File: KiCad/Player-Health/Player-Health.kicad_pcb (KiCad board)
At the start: 2 copper layers, 34 parts, among them IC1 ATMEGA328-P, J1 MICRO_USB, M1 RUMBLE, P1 2P_CGRID_M, P2 6pM CGrid, P3 6pM Header, P4 8pF Header, Q1 NPN, U1 MCP73831, U2 LM1084IT-3.3/NOPB, U3 14SLED, U4 ESP8266, X1 CRYSTAL

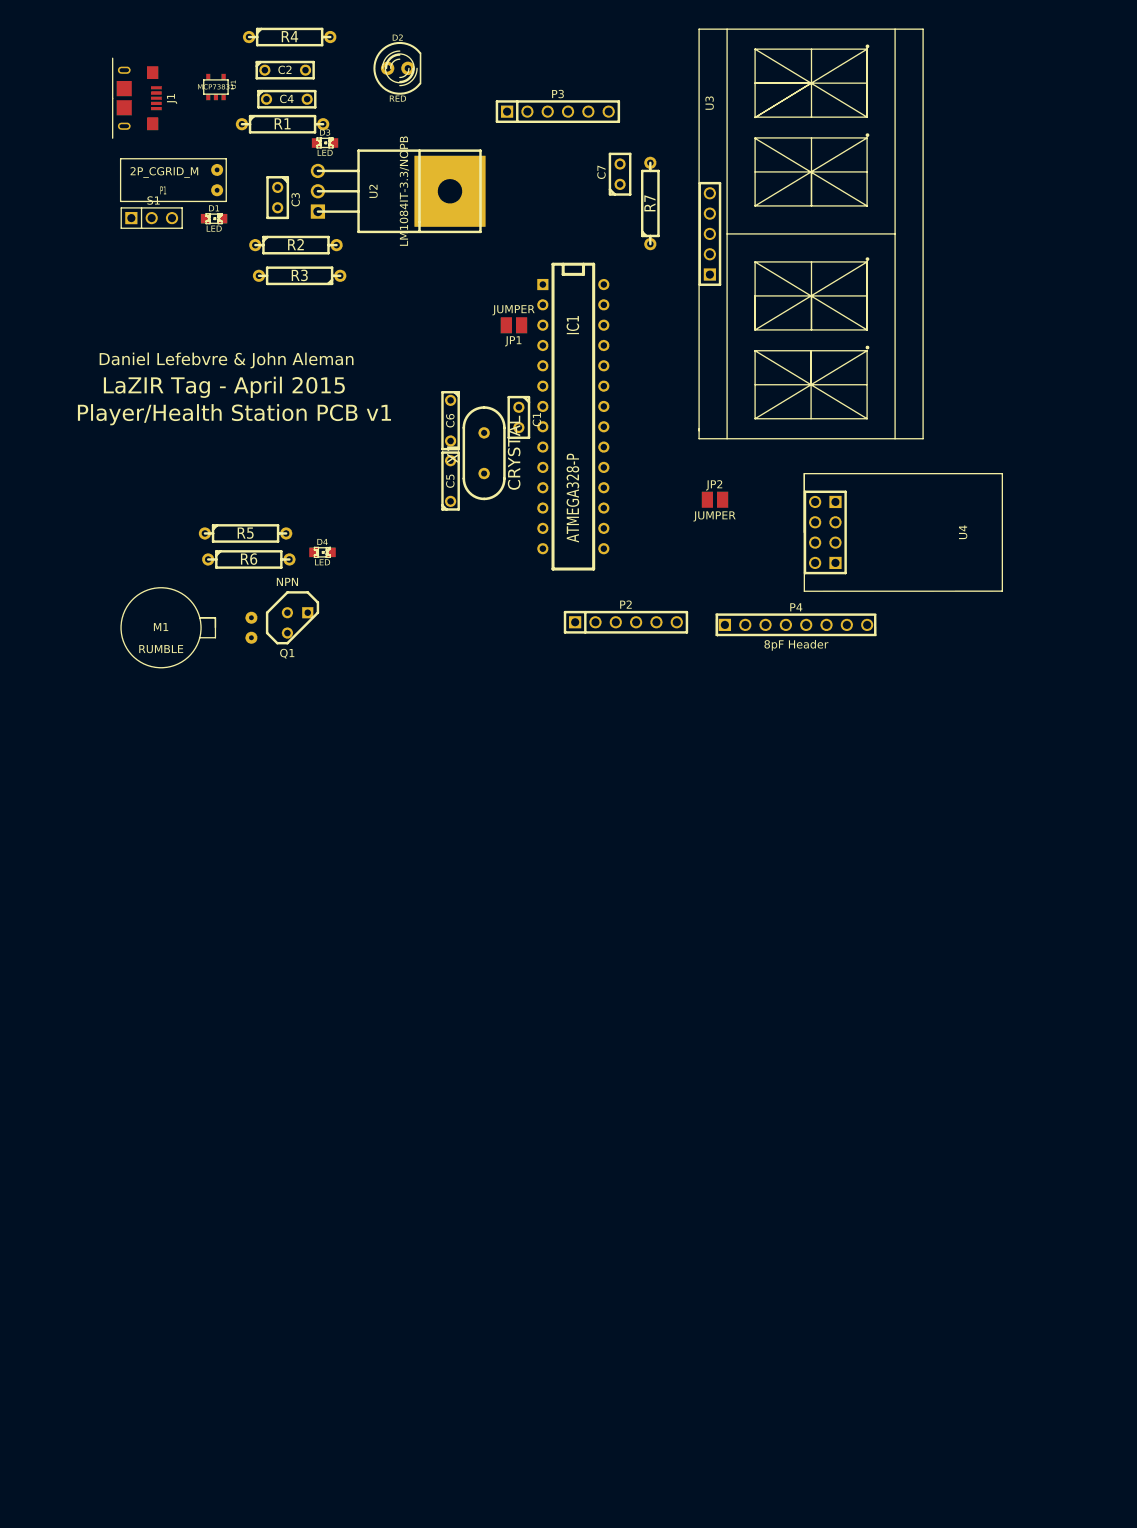
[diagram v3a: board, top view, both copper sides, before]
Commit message: Update #1 4/17
First Draft of Player/Health PCB for review.
Added on/off indicators to weapon pcb for slideswitch
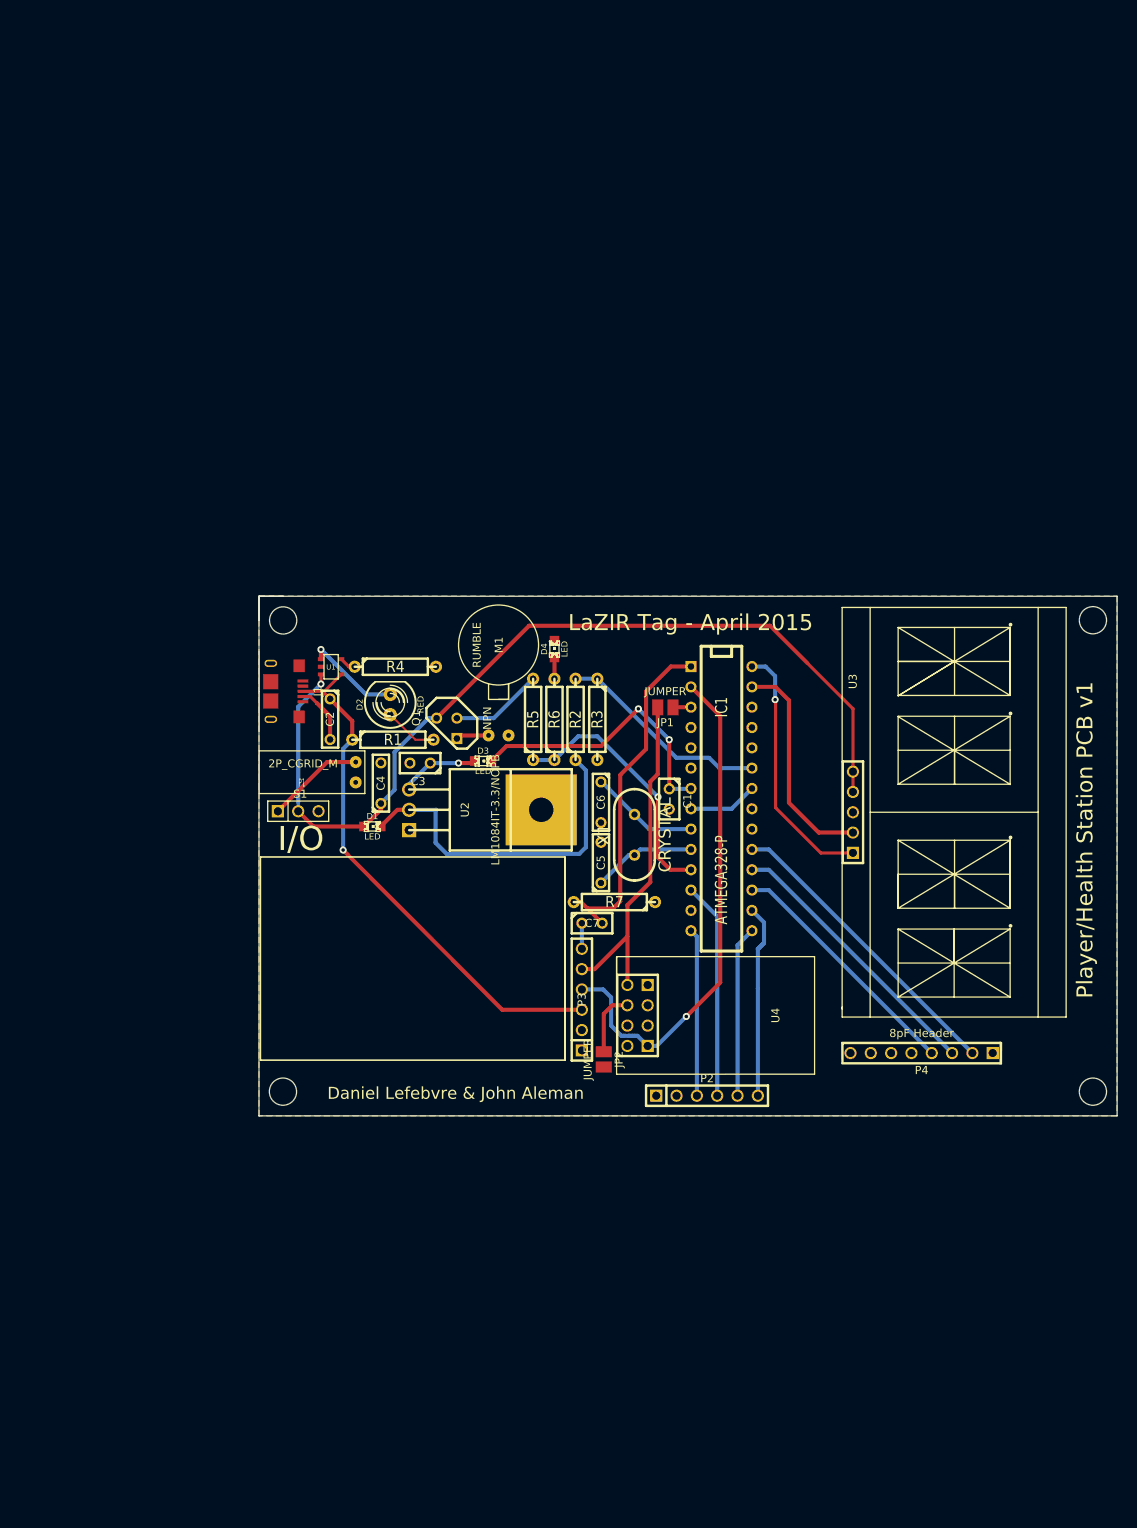
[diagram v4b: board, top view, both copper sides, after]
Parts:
- moved P3 111.0 mm to (80.7, 137.1), turned to 90 degrees
- moved C7 93.7 mm to (82.0, 127.5), turned to 0 degrees
- moved R7 87.4 mm to (84.8, 124.9), turned to 180 degrees
- moved C4 86.3 mm to (55.6, 110.0), turned to 90 degrees
- moved C2 81.3 mm to (49.3, 102.0), turned to 270 degrees
- moved R4 79.8 mm to (57.4, 95.5)
- moved D3 79.8 mm to (68.4, 107.3)
- moved D2 79.5 mm to (56.8, 100.2), turned to 90 degrees
- moved D1 78.5 mm to (54.5, 115.4)
- moved R1 78.2 mm to (57.1, 104.6)
- moved U2 78.2 mm to (59.1, 113.4)
- moved J1 76.4 mm to (41.8, 98.6)
- moved S1 76.4 mm to (45.3, 113.5)
- moved P1 76.0 mm to (52.5, 108.7)
- moved U3 74.5 mm to (114.6, 113.7)
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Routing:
- net VBatt: track 0.00 -> 116.7 mm, vias 0 -> 1
- net UART RX: track 0.00 -> 65.9 mm, vias 0 -> 1
- net USBV: track 0.00 -> 65.7 mm, vias 0 -> 1
- net UART TX: track 0.00 -> 43.6 mm
- net Reset: track 0.00 -> 43.6 mm
- net N-000006: track 0.00 -> 43.1 mm
- net SCK: track 0.00 -> 38.1 mm
- net +3.3V: track 0.00 -> 35.4 mm, vias 0 -> 2
- net MISO: track 0.00 -> 34.5 mm
- net Rumble: track 0.00 -> 32.3 mm, vias 0 -> 1
- net I2C CLK: track 0.00 -> 31.9 mm, vias 0 -> 1
- net MOSI: track 0.00 -> 30.9 mm
- net I2C DAT: track 0.00 -> 27.7 mm
- net LED G: track 0.00 -> 27.1 mm
- net VSense: track 0.00 -> 26.7 mm
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- added copper zone on B.Cu, net +3.3V
- added copper zone on F.Cu, net GND
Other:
- board outline added: 107.3 x 64.9 mm
- net class Default: trace_width 0.254 -> 0.391
- board text added: "I/O"

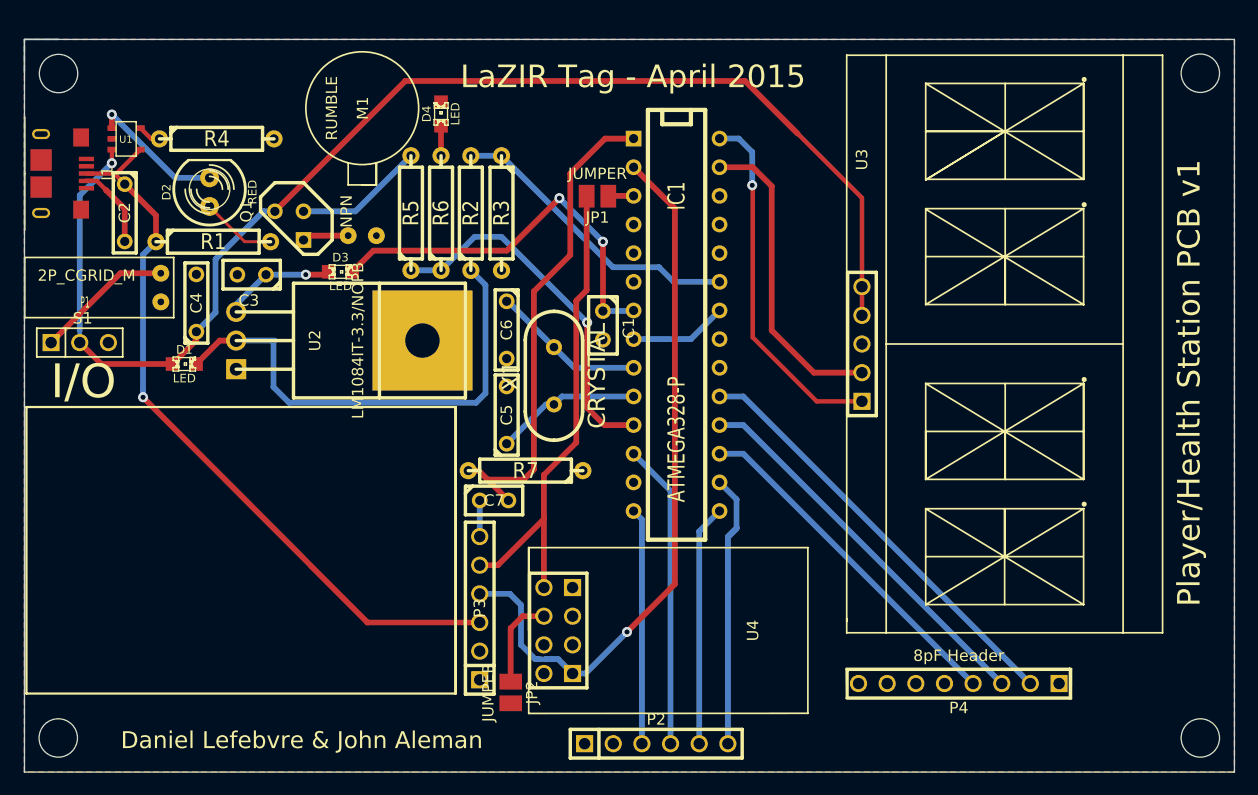
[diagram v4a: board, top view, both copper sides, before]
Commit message: Update #2 4/17
Shrunk board to be >10cm
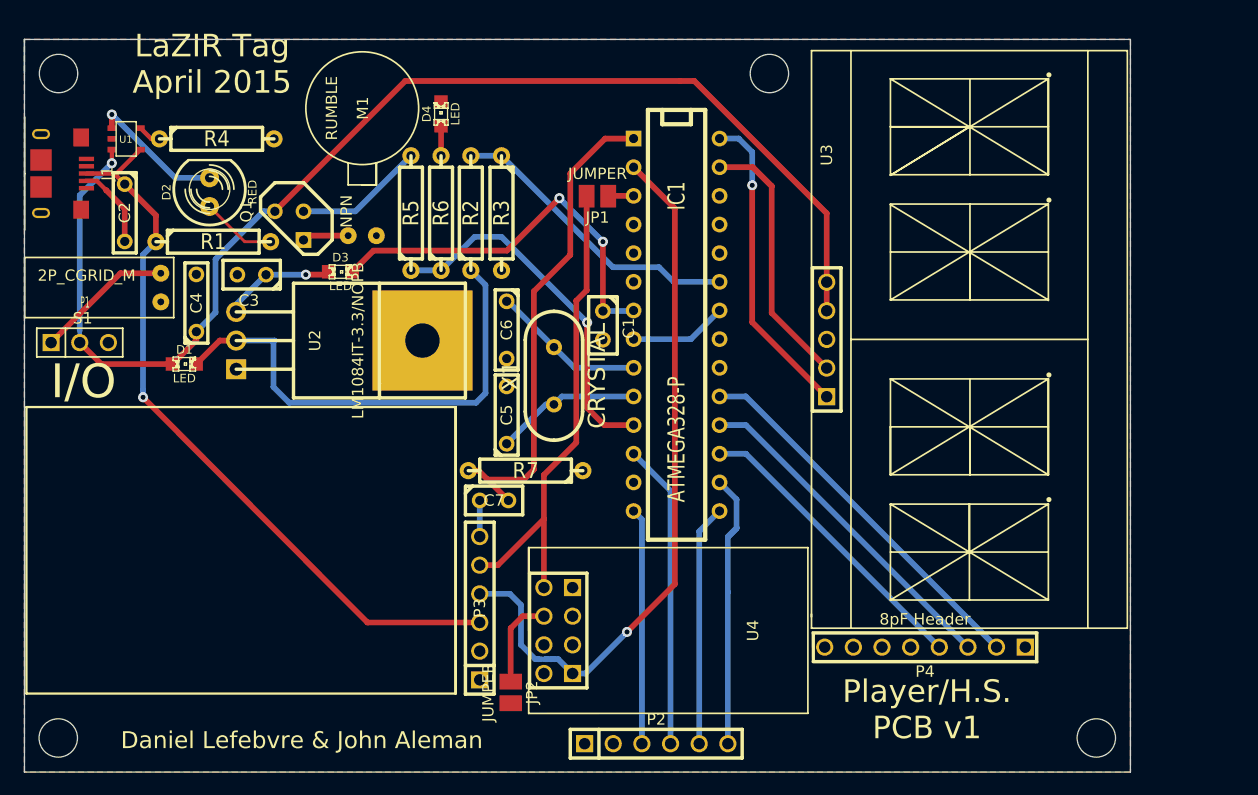
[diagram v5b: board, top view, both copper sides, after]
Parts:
- moved P4 4.40 mm to (120.2, 140.5)
- moved U3 3.15 mm to (111.5, 113.3)
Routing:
- net SCK: track 38.1 -> 65.2 mm
- net MISO: track 34.5 -> 58.0 mm
- net MOSI: track 30.9 -> 50.8 mm
- net VBatt: track 116.7 -> 129.0 mm
- net I2C CLK: track 31.9 -> 27.8 mm
- net I2C DAT: track 27.7 -> 25.8 mm
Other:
- board size 107.3 x 64.9 mm -> 98 x 64.9 mm
- net class Default: trace_width 0.391 -> 0.508
- board text added: "LaZIR Tag April 2015"
- board text added: "Player/H.S. PCB v1"
- board text removed: "LaZIR Tag - April 2015"
- board text removed: "Player/Health Station PCB v1"

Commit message: Quick Update #1 4/24
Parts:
- added R8: 220, R4, F.Cu at (87.9, 92.7)
- moved D3 22.4 mm to (87.5, 95.6)
- moved P4 5.01 mm to (124.7, 142.8)
- moved S1 0.05 mm to (45.3, 113.6)
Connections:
- C3 pad 1: N-0000028 -> +3.3V
- D3 pad 1: N-0000028 -> +3.3V
- D3 pad 2: +3.3V -> N-0000023
- U2 pad 2: N-0000028 -> +3.3V
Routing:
- net SCK: track 65.2 -> 39.2 mm
- net MISO: track 58.0 -> 35.6 mm
- net MOSI: track 50.8 -> 32.0 mm
- net +3.3V: track 35.4 -> 53.2 mm, vias 2 -> 3
- net N-0000028: track 10.1 -> 0.00 mm, vias 1 -> 0
- net N-0000023: track 0.00 -> 5.64 mm

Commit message: Quick Update #2 4/24
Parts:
- removed D1: LED, LED-0805
- moved S1 1.40 mm to (45.3, 115.0)
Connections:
- R2 pad 1: N-000005 (its old number) -> VBatt
- R3 pad 1: VSense -> (no net)
- U2 pad 3: N-000005 (its old number) -> VBatt
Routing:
- net VBatt: track 129.0 -> 172.4 mm
- net N-000005 (its old number): track 43.1 -> 0.00 mm
- net N-000005: track 12.3 -> 13.7 mm

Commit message: Quick Update #3 4/24
Adjusted keepout areas
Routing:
- net GND: track 16.0 -> 27.6 mm
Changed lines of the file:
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@@
     (links 76)
     (no_connects 0)
-    (area 39.053912 86.614799 138.459601 152.1206)
+    (area 39.104712 86.614799 138.459601 152.1206)
     (thickness 1.6)
     (drawings 23)
-    (tracks 183)
+    (tracks 186)
     (zones 0)
     (modules 34)
@@
   (segment (start 61.7728 107.5182) (end 65.3034 107.5182) (width 0.508) (layer B.Cu) (net 1))
   (via (at 65.3034 107.5182) (size 0.889) (layers F.Cu B.Cu) (net 1))
+  (segment (start 59.1312 115.9002) (end 54.2544 115.9002) (width 0.508) (layer B.Cu) (net 2) (status 400000))
+  (segment (start 52.451 114.0968) (end 52.451 109.9312) (width 0.508) (layer B.Cu) (net 2) (status 800000))
+  (segment (start 54.2544 115.9002) (end 52.451 114.0968) (width 0.508) (layer B.Cu) (net 2))
   (segment (start 94.361 113.2332) (end 99.441 113.2332) (width 0.508) (layer B.Cu) (net 2))
   (segment (start 99.441 113.2332) (end 101.981 110.6932) (width 0.508) (layer B.Cu) (net 2))
@@
       )
     )
+  )
+  (zone (net 0) (net_name "") (layer B.Cu) (hatch edge 0.508)
+    (connect_pads (clearance 0.508))
+    (min_thickness 0.254)
+    (keepout (tracks not_allowed) (vias not_allowed) (copperpour not_allowed))
+    (fill (arc_segments 16) (thermal_gap 0.508) (thermal_bridge_width 0.508))
+    (polygon
+      (pts
+        (xy 80.6704 133.223) (xy 80.7466 127.762) (xy 85.7504 125.8062) (xy 85.979 128.8034) (xy 81.9404 133.1722)
+      )
+    )
+  )
+  (zone (net 0) (net_name "") (layer F.Cu) (hatch edge 0.508)
+    (connect_pads (clearance 0.508))
+    (min_thickness 0.254)
+    (keepout (tracks not_allowed) (vias not_allowed) (copperpour not_allowed))
+    (fill (arc_segments 16) (thermal_gap 0.508) (thermal_bridge_width 0.508))
+    (polygon
+      (pts
+        (xy 80.6704 133.223) (xy 80.7466 127.762) (xy 85.7504 125.8062) (xy 85.979 128.8034) (xy 81.9404 133.1722)
+      )
+    )
+  )
+  (zone (net 0) (net_name "") (layer B.Cu) (hatch edge 0.508)
+    (connect_pads (clearance 0.508))
+    (min_thickness 0.254)
+    (keepout (tracks not_allowed) (vias not_allowed) (copperpour not_allowed))
+    (fill (arc_segments 16) (thermal_gap 0.508) (thermal_bridge_width 0.508))
+    (polygon
+      (pts
+        (xy 42.9514 115.0874) (xy 42.9514 113.538) (xy 49.022 107.4674) (xy 51.3588 107.4166) (xy 51.0032 112.4458)
+        (xy 47.0408 112.4966) (xy 45.2374 114.9604)
+      )
+    )
+  )
+  (zone (net 0) (net_name "") (layer F.Cu) (hatch edge 0.508)
+    (connect_pads (clearance 0.508))
+    (min_thickness 0.254)
+    (keepout (tracks not_allowed) (vias not_allowed) (copperpour not_allowed))
+    (fill (arc_segments 16) (thermal_gap 0.508) (thermal_bridge_width 0.508))
+    (polygon
+      (pts
+        (xy 42.9514 115.0874) (xy 42.9514 113.538) (xy 49.022 107.4674) (xy 51.3588 107.4166) (xy 51.0032 112.4458)
+        (xy 47.0408 112.4966) (xy 45.2374 114.9604)
+      )
+    )
+  )
+  (zone (net 0) (net_name "") (layer B.Cu) (hatch edge 0.508)
+    (connect_pads (clearance 0.508))
+    (min_thickness 0.254)
+    (keepout (tracks not_allowed) (vias not_allowed) (copperpour not_allowed))
+    (fill (arc_segments 16) (thermal_gap 0.508) (thermal_bridge_width 0.508))
+    (polygon
+      (pts
+        (xy 93.8022 120.8278) (xy 91.7194 120.904) (xy 90.2208 119.3546) (xy 90.17 114.4524) (xy 93.8784 114.5286)
+        (xy 93.8784 114.7064)
+      )
+    )
+  )
+  (zone (net 0) (net_name "") (layer F.Cu) (hatch edge 0.508)
+    (connect_pads (clearance 0.508))
+    (min_thickness 0.254)
+    (keepout (tracks not_allowed) (vias not_allowed) (copperpour not_allowed))
+    (fill (arc_segments 16) (thermal_gap 0.508) (thermal_bridge_width 0.508))
+    (polygon
+      (pts
+        (xy 93.8022 120.8278) (xy 91.7194 120.904) (xy 90.2208 119.3546) (xy 90.17 114.4524) (xy 93.8784 114.5286)
+        (xy 93.8784 114.7064)
+      )
+    )
